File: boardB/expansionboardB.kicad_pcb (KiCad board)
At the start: 4 copper layers, 131 x 83.8 mm, 58 parts, among them J1 USB_C_Receptacle, J3 HDMI_A, SW4 ESPPROG, U1 ESP32-S3-WROOM-1, U2 GPIO_U2, U4 GPIO_U4, U5 SII1136CTU, U7 MAX20022ATIA+T, t1V2 1V2_TEST, t3V3 3V3_TEST

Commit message: Board updates
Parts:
- added R15: 10K0, Resistor_SMD:R_0603_1608Metric_Pad0.98x0.95mm_HandSolder, B.Cu at (89.7, 64.4)
- added R16: 3K0, Resistor_SMD:R_0603_1608Metric_Pad0.98x0.95mm_HandSolder, B.Cu at (89.7, 62.4)
- R1: value 23K0 -> 10K0
- R10: value 23K0 -> 2K0
- R9: value 4K06 -> 4K02
- moved R12 3.72 mm to (84.6, 66.3)
- moved C1 1.93 mm to (89.7, 60.3)
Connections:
- R1 pad 1: /VOUT_1 -> Net-(R1-Pad1)
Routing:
- net /OUTS_1: track 10.7 -> 17.0 mm
- net Net-(R15-Pad1): track 0.00 -> 2.04 mm
- net Net-(R1-Pad1): track 0.00 -> 2.02 mm
- net /VOUT_1: track 11.7 -> 12.7 mm

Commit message: Board updates
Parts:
- removed E1 (x5): SparkGap, Diode_SMD:D_0201_0603Metric
- added D1: LED, LED_SMD:LED_1206_3216Metric_Pad1.42x1.75mm_HandSolder, B.Cu at (24.9, 78.9)
- added R17: 33, Resistor_SMD:R_0603_1608Metric_Pad0.98x0.95mm_HandSolder, B.Cu at (32.8, 78.9)
- added SW1: ESPRST, Button_Switch_SMD:SW_Tactile_SPST_NO_Straight_CK_PTS636Sx25SMTRLFS, B.Cu at (86.6, 47.4)
- added t5V1: 5V_IN_TEST, TestPoint:TestPoint_Pad_D1.5mm, B.Cu at (68.6, 74.2)
- added tDIAG1: DIAGNOSIS, TestPoint:TestPoint_Pad_D1.5mm, B.Cu at (100.8, 114.3)
- added tPG1: PG1_TEST, TestPoint:TestPoint_Pad_D1.5mm, B.Cu at (80.1, 84.3)
- added tPG2: PG2_TEST, TestPoint:TestPoint_Pad_D1.5mm, B.Cu at (76.5, 84.3)
- JTAG1: moved to B.Cu
- moved t3V3 18.5 mm to (80.4, 61.2)
- moved t1V2 6.18 mm to (100.1, 88.5)
- turned JTAG1 to 90 degrees
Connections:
- U2 pad 36: unconnected-(U2-Pin_36-Pad36) -> LEDPWR
- U4 pad 8: unconnected-(U4-Pin_8-Pad8) -> Net-(U4-Pin_8)
- U7 pad 10: unconnected-(U7-PG2-Pad10) -> Net-(U7-PG2)
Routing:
- net SHLD: track 37.8 -> 24.0 mm
- net LEDPWR: track 0.00 -> 12.0 mm
- net Net-(U7-PG2): track 0.00 -> 12.0 mm
- net /PG_1: track 12.6 -> 22.9 mm
- net ESP_RST: track 51.3 -> 59.0 mm
- net Net-(U4-Pin_8): track 0.00 -> 5.84 mm
- net Net-(D1-A): track 0.00 -> 5.56 mm
- net 5V: track 17.2 -> 18.9 mm, vias 4 -> 5
- net REG1V2: track 22.5 -> 21.6 mm, vias 8 -> 9
- net REG3V3: track 30.3 -> 29.6 mm, vias 7 -> 8
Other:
- board text added: "RESET"

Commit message: board update
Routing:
- net D_HPD: track 27.1 -> 26.2 mm
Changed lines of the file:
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@@
 		)
 		(property "Value" "33"
-			(at -5.3895 -0.127 360)
+			(at -5.3895 -0.127 0)
 			(layer "B.Fab")
 			(effects
@@
 		)
 		(fp_text user "${REFERENCE}"
-			(at 0 0 360)
+			(at 0 0 0)
 			(layer "B.Fab")
 			(effects
@@
 		)
 		(property "Value" "LED"
-			(at 0 -1.82 360)
+			(at 0 -1.82 0)
 			(layer "B.Fab")
 			(effects
@@
 		)
 		(fp_text user "${REFERENCE}"
-			(at 0 0 360)
+			(at 0 0 0)
 			(layer "B.Fab")
 			(effects
@@
 	)
 	(via
-		(at 24.13 88.9)
+		(at 23.749 88.9)
 		(size 0.8)
 		(drill 0.4)
@@
 	)
 	(via
-		(at 129.889898 79.92677)
+		(at 132.334 81.153)
 		(size 0.8)
 		(drill 0.4)
@@
 	)
 	(segment
-		(start 143.852107 75.349893)
-		(end 139.568123 79.633877)
+		(start 132.334 81.153)
+		(end 132.974444 80.512556)
 		(width 0.2)
 		(layer "In2.Cu")
@@
 	)
 	(segment
-		(start 144.92 65.84)
+		(start 144.437893 66.001107)
 		(end 144.599 65.84)
 		(width 0.2)
@@
 	)
 	(segment
-		(start 144.599 65.84)
-		(end 144.437893 66.001107)
+		(start 139.568123 79.633877)
+		(end 143.852107 75.349893)
 		(width 0.2)
 		(layer "In2.Cu")
@@
 	)
 	(segment
-		(start 144.145 66.708214)
-		(end 144.145 74.642786)
+		(start 134.388657 79.92677)
+		(end 138.861016 79.92677)
 		(width 0.2)
 		(layer "In2.Cu")
@@
 	)
 	(segment
-		(start 138.861016 79.92677)
-		(end 129.889898 79.92677)
+		(start 144.145 74.642786)
+		(end 144.145 66.708214)
 		(width 0.2)
 		(layer "In2.Cu")
 		(net 15)
 	)
-	(arc
-		(start 144.145 74.642786)
-		(mid 144.06888 75.025469)
-		(end 143.852107 75.349893)
+	(segment
+		(start 144.599 65.84)
+		(end 144.92 65.84)
 		(width 0.2)
 		(layer "In2.Cu")
@@
 	)
 	(arc
+		(start 134.388657 79.92677)
+		(mid 133.62329 80.079011)
+		(end 132.974444 80.512556)
+		(width 0.2)
+		(layer "In2.Cu")
+		(net 15)
+	)
+	(arc
 		(start 144.145 66.708214)
 		(mid 144.22112 66.325531)
@@
 		(net 15)
 	)
+	(arc
+		(start 143.852107 75.349893)
+		(mid 144.06888 75.025469)
+		(end 144.145 74.642786)
+		(width 0.2)
+		(layer "In2.Cu")
+		(net 15)
+	)
 	(segment
-		(start 129.889898 81.114898)
+		(start 132.331 81.15)
 		(end 129.925 81.15)
 		(width 0.25)
@@
 	)
 	(segment
-		(start 129.889898 79.92677)
-		(end 129.889898 81.114898)
+		(start 132.334 81.153)
+		(end 132.331 81.15)
 		(width 0.25)
 		(layer "B.Cu")
@@
 	)
 	(segment
-		(start 33.492 91.15)
-		(end 33.528 91.186)
-		(width 0.25)
-		(layer "B.Cu")
-		(net 31)
-	)
-	(segment
 		(start 90.678 78.486)
 		(end 88.317 76.125)
@@
 		(polygon
 			(pts
-				(xy 135.128 40.386) (xy 135.128 44.704) (xy 133.096 44.704) (xy 133.096 61.087) (xy 135.763 61.087)
-				(xy 135.763 66.802) (xy 135.763 79.121) (xy 129.032 79.121) (xy 129.032 115.062) (xy 133.731 115.062)
+				(xy 133.096 40.386) (xy 133.096 44.704) (xy 133.096 44.704) (xy 133.096 60.452) (xy 135.763 60.452)
+				(xy 135.763 66.802) (xy 135.763 78.994) (xy 129.032 78.994) (xy 129.032 115.062) (xy 133.731 115.062)
 				(xy 133.731 122.174) (xy 127.127 122.174) (xy 127.127 117.475) (xy 127.127 76.073) (xy 130.81 76.073)
-				(xy 130.81 74.295) (xy 125.857 74.295) (xy 125.857 84.836) (xy 120.015 84.836) (xy 120.015 91.059)
-				(xy 86.995 91.059) (xy 86.995 86.614) (xy 86.995 82.169) (xy 86.995 77.47) (xy 30.734 77.47) (xy 30.734 93.091)
-				(xy 25.146 93.091) (xy 25.146 85.09) (xy 28.829 85.09) (xy 28.829 75.311) (xy 31.75 75.311) (xy 31.75 47.117)
+				(xy 130.81 74.295) (xy 125.73 74.295) (xy 125.73 84.836) (xy 120.015 84.836) (xy 120.015 91.059)
+				(xy 86.995 91.059) (xy 86.995 86.614) (xy 86.995 82.169) (xy 86.995 77.47) (xy 30.988 77.47) (xy 30.988 93.091)
+				(xy 25.019 93.091) (xy 25.019 85.09) (xy 28.829 85.09) (xy 28.829 75.311) (xy 31.75 75.311) (xy 31.75 47.117)
 				(xy 42.926 47.117) (xy 42.926 40.386) (xy 21.336 40.386) (xy 21.336 125.476) (xy 153.67 125.476)
 				(xy 153.67 40.386)
@@
 			(pts
 				(xy 127.508 117.094) (xy 127.508 121.793) (xy 133.35 121.793) (xy 133.35 115.443) (xy 128.651 115.443)
-				(xy 128.651 78.74) (xy 135.382 78.74) (xy 135.382 61.468) (xy 121.285 61.468) (xy 121.285 62.357)
-				(xy 93.599 62.357) (xy 93.599 43.561) (xy 65.786 43.561) (xy 62.23 43.561) (xy 52.07 43.561) (xy 50.292 43.561)
+				(xy 128.651 78.613) (xy 135.382 78.613) (xy 135.382 60.833) (xy 121.285 60.833) (xy 121.285 62.357)
+				(xy 93.599 62.357) (xy 93.599 44.704) (xy 65.786 44.704) (xy 62.738 44.704) (xy 52.578 44.704) (xy 50.292 44.704)
 				(xy 50.292 49.276) (xy 50.292 51.054) (xy 36.195 51.054) (xy 36.195 64.262) (xy 92.964 64.262) (xy 92.964 79.756)
 				(xy 113.157 79.756) (xy 113.157 81.915) (xy 122.682 81.915) (xy 122.682 78.359) (xy 116.459 78.359)
@@
 		(polygon
 			(pts
-				(xy 123.825 56.896) (xy 123.825 44.704) (xy 93.98 44.704) (xy 93.98 61.976) (xy 120.904 61.976)
+				(xy 120.904 56.896) (xy 120.904 44.704) (xy 93.98 44.704) (xy 93.98 61.976) (xy 120.904 61.976)
 				(xy 120.904 56.896)
 			)
@@
 			(pts
 				(xy 87.376 77.089) (xy 87.376 79.756) (xy 92.583 79.756) (xy 92.583 64.643) (xy 49.784 64.643) (xy 35.814 64.643)
-				(xy 35.814 56.515) (xy 35.814 50.673) (xy 49.911 50.673) (xy 49.911 49.022) (xy 49.911 43.18) (xy 93.98 43.18)
-				(xy 93.98 44.323) (xy 124.206 44.323) (xy 124.206 57.277) (xy 121.285 57.277) (xy 121.285 61.087)
-				(xy 132.715 61.087) (xy 132.715 44.323) (xy 134.747 44.323) (xy 134.747 40.386) (xy 43.307 40.386)
-				(xy 43.307 47.498) (xy 32.131 47.498) (xy 32.131 75.692) (xy 29.21 75.692) (xy 29.21 85.471) (xy 25.527 85.471)
-				(xy 25.527 92.71) (xy 30.353 92.71) (xy 30.353 77.089) (xy 87.122 77.089)
+				(xy 35.814 56.515) (xy 35.814 50.673) (xy 49.911 50.673) (xy 49.911 49.022) (xy 49.911 44.323) (xy 93.98 44.323)
+				(xy 93.98 44.323) (xy 121.285 44.323) (xy 121.285 57.277) (xy 121.285 57.277) (xy 121.285 60.452)
+				(xy 132.715 60.452) (xy 132.715 44.323) (xy 132.715 44.323) (xy 132.715 40.386) (xy 43.307 40.386)
+				(xy 43.307 47.498) (xy 32.131 47.498) (xy 32.131 75.692) (xy 29.21 75.692) (xy 29.21 85.471) (xy 25.4 85.471)
+				(xy 25.4 92.71) (xy 30.607 92.71) (xy 30.607 77.089) (xy 87.122 77.089)
 			)
 		)
@@
 				(xy 123.063 77.978) (xy 116.84 77.978) (xy 116.84 74.422) (xy 119.126 74.422) (xy 119.126 72.136)
 				(xy 116.84 72.136) (xy 116.84 66.802) (xy 122.936 66.802) (xy 130.81 66.802) (xy 130.81 73.914)
-				(xy 125.476 73.914) (xy 125.476 84.455) (xy 119.634 84.455) (xy 119.634 90.678) (xy 87.376 90.678)
+				(xy 125.349 73.914) (xy 125.349 84.455) (xy 119.634 84.455) (xy 119.634 90.678) (xy 87.376 90.678)
 				(xy 87.376 82.55) (xy 87.376 80.137) (xy 112.776 80.137) (xy 112.776 82.296) (xy 123.063 82.296)
 			)

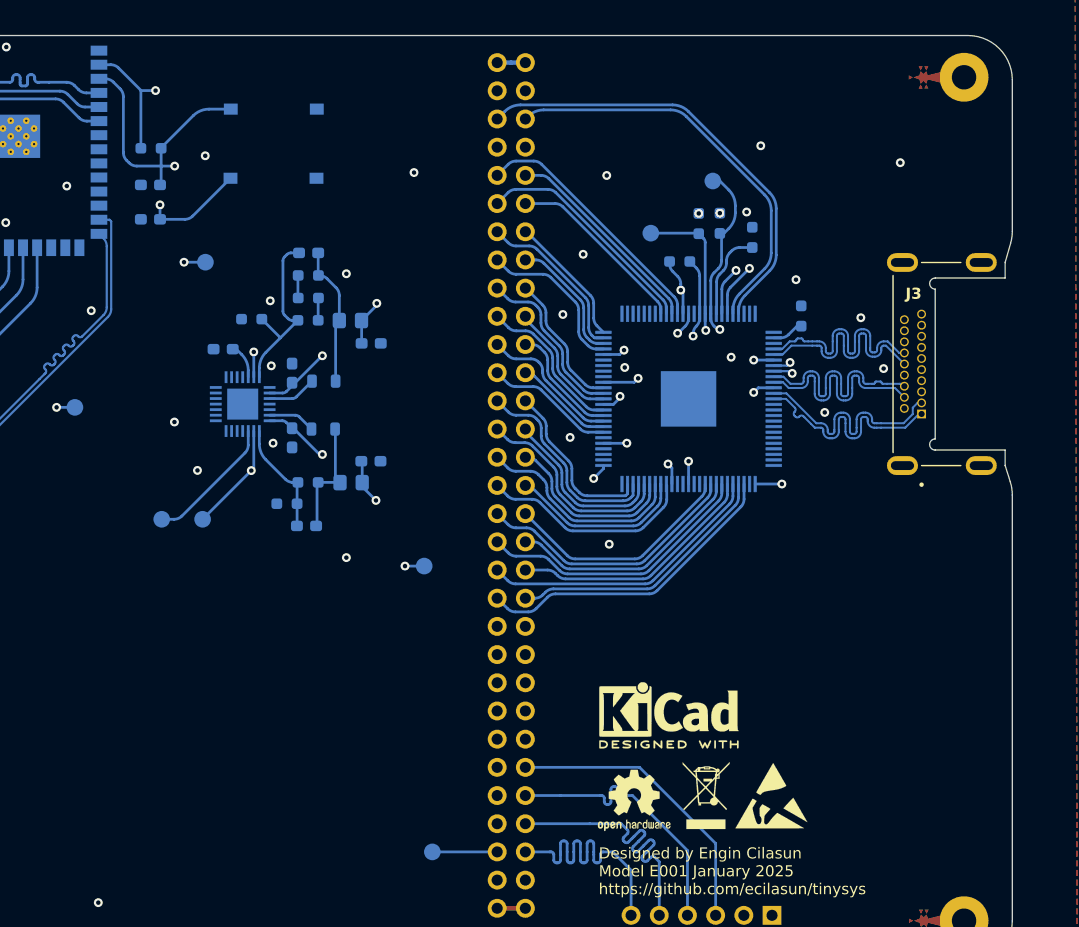
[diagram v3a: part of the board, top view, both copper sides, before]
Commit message: Started to get rid of the video and audio chips and circuitry
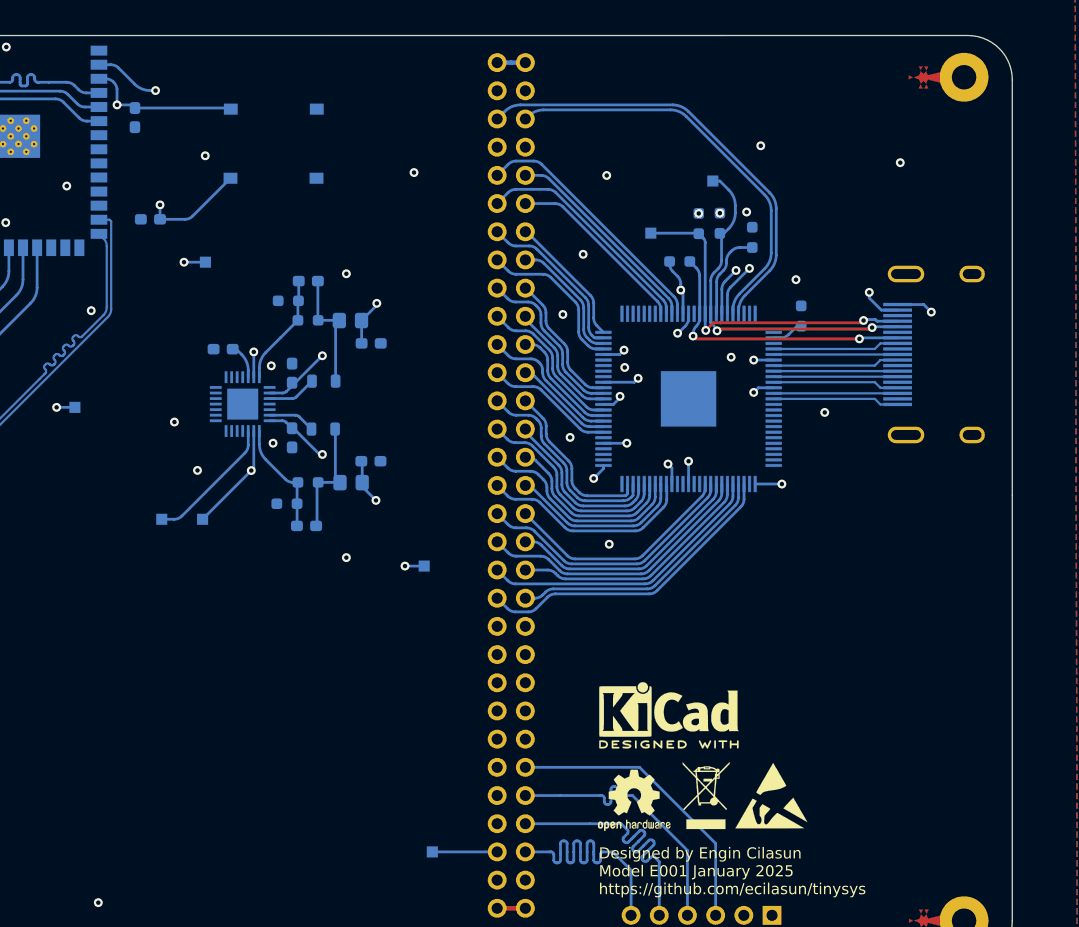
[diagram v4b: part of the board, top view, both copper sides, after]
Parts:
- removed J3: HDMI_A, HD02-19-M-MSMT-TR:CUI_HD02-19-M-MSMT-TR
- removed R15, R2: 10K0, Resistor_SMD:R_0603_1608Metric_Pad0.98x0.95mm_HandSolder
- removed R16: 3K0, Resistor_SMD:R_0603_1608Metric_Pad0.98x0.95mm_HandSolder
- added J2: 2086581051, HDMI_2086:MOLEX_2086581051, B.Cu at (153.1, 69.5)
- R1: value 10K0 -> 23K0
- t1V2, t3V3, t5V1, tDIAG1, tPG1, tPG2, tSCL1, tSDA1: footprint TestPoint:TestPoint_Pad_D1.5mm -> TestPoint:TestPoint_Pad_1.0x1.0mm
- moved C4 6.23 mm to (74.0, 48.1), turned to -90 degrees
- moved R12 3.69 mm to (87.9, 64.6)
- moved C1 2.54 mm to (89.7, 62.9)
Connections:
- R1 pad 1: Net-(R1-Pad1) -> /VOUT_1
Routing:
- net ESP_RST: track 59.0 -> 41.2 mm
- net D2_N: track 21.3 -> 11.2 mm
- net D1_N: track 21.3 -> 11.2 mm
- net CK_P: track 21.3 -> 11.2 mm
- net D2_P: track 21.3 -> 11.4 mm
- net D1_P: track 21.3 -> 11.4 mm
- net CK_N: track 21.3 -> 11.4 mm
- net D0_P: track 20.0 -> 11.2 mm, vias 1 -> 0
- net D_CEC: track 34.4 -> 25.8 mm, vias 1 -> 2
- net D0_N: track 20.0 -> 11.4 mm, vias 1 -> 0
- net D_HPD: track 26.2 -> 33.9 mm, vias 1 -> 2
- net /OUTS_1: track 17.0 -> 10.0 mm
- net REG3V3: track 29.6 -> 24.3 mm
- net D_SCL: track 36.3 -> 32.3 mm, vias 1 -> 2
- net 5V: track 18.8 -> 22.4 mm, vias 5 -> 6
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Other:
- outline, holes or cut-outs redrawn
- board text added: "A/V"
- board text added: "COM"
- board text added: "JTAG"
- board text added: "POW / DAT"
- board text added: "REG"
- board text removed: "ESP32-S3-WROOM-1"
- board text removed: "POWER & DATA"

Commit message: Updates to board and mechanical files Rebuilt tinyremote exe Updated device with WNS fixes
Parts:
- added E1: SparkGap, Diode_SMD:D_0201_0603Metric, F.Cu at (0.96, 0.38)
- R1: value 23K0 -> 11K5
- R12: value 10K0 -> 5K0
